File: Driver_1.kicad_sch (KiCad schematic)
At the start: 34 parts

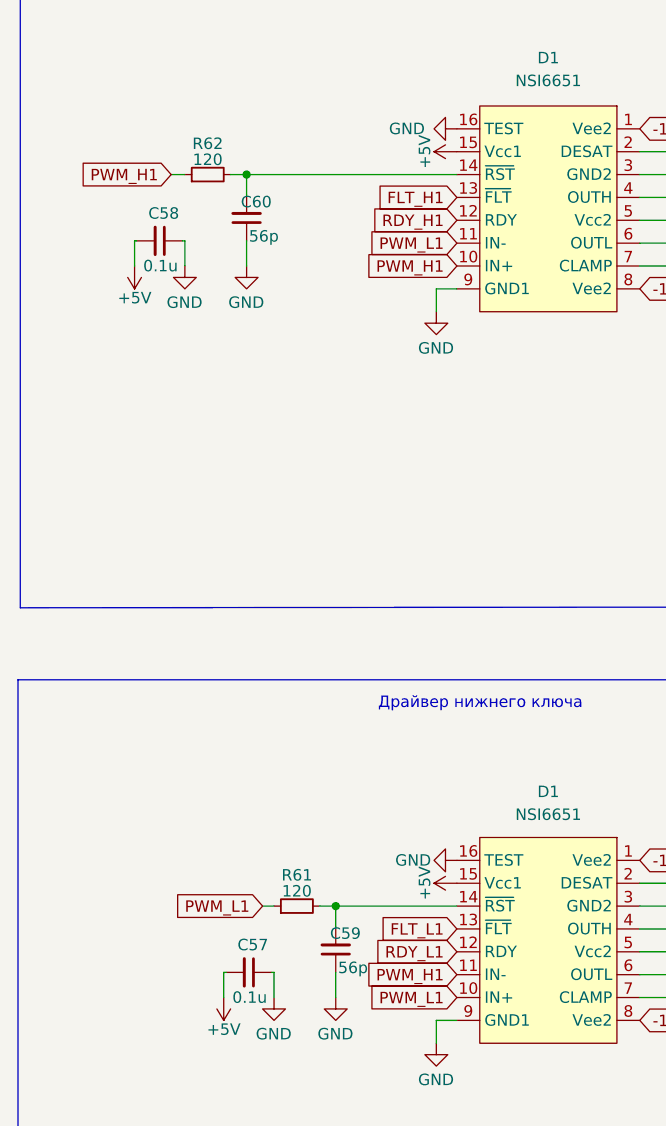
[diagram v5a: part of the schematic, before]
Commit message: Развел стойку фазы А
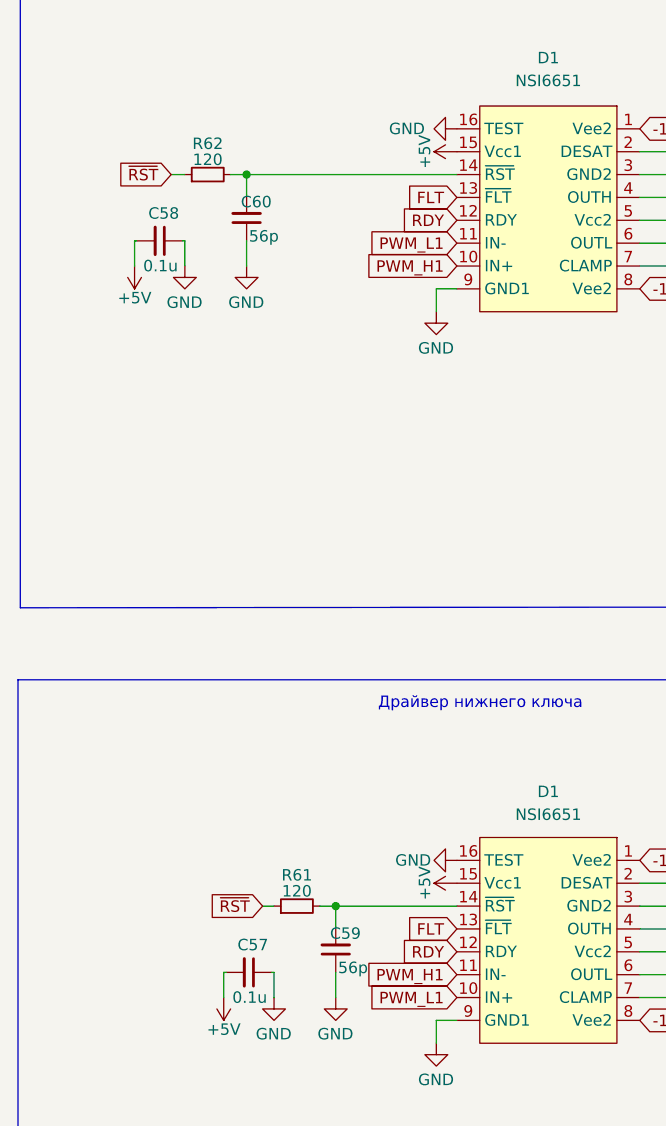
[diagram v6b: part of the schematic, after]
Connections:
- net FLT_L1 is gone; now on net FLT: D1.13 (~{FLT})
- net RDY_L1 is gone; now on net RDY: D1.12 (RDY)
- net PWM_H1: no longer R62.1
- net PWM_L1: no longer R61.1
- net FLT_H1 renamed FLT
- net RDY_H1 renamed RDY
- new net ~{RST}: R61.1, R62.1
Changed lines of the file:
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@@
 		)
 	)
-	(global_label "PWM_H1"
+	(global_label "~{RST}"
 		(shape input)
 		(at 48.26 52.07 180)
@@
 		)
 		(property "Intersheetrefs" "${INTERSHEET_REFS}"
-			(at 38.1664 51.9906 0)
+			(at 42.445 52.07 0)
 			(effects
 				(font
@@
 		)
 	)
-	(global_label "RDY_H1"
+	(global_label "RDY"
 		(shape input)
 		(at 80.01 57.15 180)
@@
 		)
 		(property "Intersheetrefs" "${INTERSHEET_REFS}"
-			(at 70.4607 57.0706 0)
+			(at 74.0684 57.15 0)
 			(effects
 				(font
@@
 		)
 	)
-	(global_label "PWM_L1"
-		(shape input)
-		(at 58.42 133.35 180)
-		(fields_autoplaced yes)
-		(effects
-			(font
-				(size 1.27 1.27)
-			)
-			(justify right)
-		)
-		(property "Intersheetrefs" "${INTERSHEET_REFS}"
-			(at 48.6288 133.2706 0)
-			(effects
-				(font
-					(size 1.27 1.27)
-				)
-				(justify right)
-				(hide yes)
-			)
-		)
-	)
 	(global_label "G1"
 		(shape output)
@@
 		)
 	)
-	(global_label "FLT_H1"
+	(global_label "FLT"
 		(shape input)
 		(at 80.01 54.61 180)
@@
 		)
 		(property "Intersheetrefs" "${INTERSHEET_REFS}"
-			(at 71.005 54.5306 0)
+			(at 74.4506 54.61 0)
 			(effects
 				(font
@@
 		)
 	)
-	(global_label "FLT_L1"
+	(global_label "FLT"
 		(shape input)
 		(at 80.01 135.89 180)
@@
 		)
 		(property "Intersheetrefs" "${INTERSHEET_REFS}"
-			(at 71.3074 135.8106 0)
+			(at 74.4506 135.89 0)
+			(effects
+				(font
+					(size 1.27 1.27)
+				)
+				(justify right)
+				(hide yes)
+			)
+		)
+	)
+	(global_label "~{RST}"
+		(shape input)
+		(at 58.42 133.35 180)
+		(fields_autoplaced yes)
+		(effects
+			(font
+				(size 1.27 1.27)
+			)
+			(justify right)
+		)
+		(property "Intersheetrefs" "${INTERSHEET_REFS}"
+			(at 52.605 133.35 0)
 			(effects
 				(font
@@
 		)
 	)
-	(global_label "RDY_L1"
+	(global_label "RDY"
 		(shape input)
 		(at 80.01 138.43 180)
@@
 		)
 		(property "Intersheetrefs" "${INTERSHEET_REFS}"
-			(at 70.7631 138.3506 0)
+			(at 74.0684 138.43 0)
 			(effects
 				(font
@@
 		(on_board yes)
 		(dnp no)
-		(property "Reference" "#PWR168"
+		(property "Reference" "#PWR0168"
 			(at 83.82 49.53 0)
 			(effects
@@
 			(project "Adapter"
 				(path "/e63e39d7-6ac0-4ffd-8aa3-1841a4541b55/24ca47b2-866f-4c90-ba1b-98c358d573e6"
-					(reference "#PWR168")
+					(reference "#PWR0168")
 					(unit 1)
 				)
@@
 		(on_board yes)
 		(dnp no)
-		(property "Reference" "#PWR162"
+		(property "Reference" "#PWR0162"
 			(at 83.82 130.81 0)
 			(effects
@@
 			(project "Adapter"
 				(path "/e63e39d7-6ac0-4ffd-8aa3-1841a4541b55/24ca47b2-866f-4c90-ba1b-98c358d573e6"
-					(reference "#PWR162")
+					(reference "#PWR0162")
 					(unit 1)
 				)
@@
 		(on_board yes)
 		(dnp no)
-		(property "Reference" "#PWR167"
+		(property "Reference" "#PWR0167"
 			(at 44.196 58.42 0)
 			(effects
@@
 			(project "Adapter"
 				(path "/e63e39d7-6ac0-4ffd-8aa3-1841a4541b55/24ca47b2-866f-4c90-ba1b-98c358d573e6"
-					(reference "#PWR167")
+					(reference "#PWR0167")
 					(unit 1)
 				)
@@
 		(on_board yes)
 		(dnp no)
-		(property "Reference" "#PWR161"
+		(property "Reference" "#PWR0161"
 			(at 54.102 139.7 0)
 			(effects
@@
 			(project "Adapter"
 				(path "/e63e39d7-6ac0-4ffd-8aa3-1841a4541b55/24ca47b2-866f-4c90-ba1b-98c358d573e6"
-					(reference "#PWR161")
-					(unit 1)
-				)
+					(reference "#PWR0161")
+					(unit 1)
+				)

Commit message: Развел вторую стойку
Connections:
- net FLT renamed FLT_A
- net RDY renamed RDY_A
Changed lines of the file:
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@@
 		)
 	)
-	(global_label "RDY"
+	(global_label "RDY_A"
 		(shape input)
 		(at 80.01 57.15 180)
@@
 		)
 		(property "Intersheetrefs" "${INTERSHEET_REFS}"
-			(at 74.0684 57.15 0)
+			(at 71.34 57.15 0)
 			(effects
 				(font
@@
 		)
 	)
-	(global_label "FLT"
+	(global_label "FLT_A"
 		(shape input)
 		(at 80.01 54.61 180)
@@
 		)
 		(property "Intersheetrefs" "${INTERSHEET_REFS}"
-			(at 74.4506 54.61 0)
-			(effects
-				(font
-					(size 1.27 1.27)
-				)
-				(justify right)
-				(hide yes)
-			)
-		)
-	)
-	(global_label "FLT"
+			(at 71.8843 54.61 0)
+			(effects
+				(font
+					(size 1.27 1.27)
+				)
+				(justify right)
+				(hide yes)
+			)
+		)
+	)
+	(global_label "FLT_A"
 		(shape input)
 		(at 80.01 135.89 180)
@@
 		)
 		(property "Intersheetrefs" "${INTERSHEET_REFS}"
-			(at 74.4506 135.89 0)
+			(at 71.8843 135.89 0)
 			(effects
 				(font
@@
 		)
 	)
-	(global_label "RDY"
+	(global_label "RDY_A"
 		(shape input)
 		(at 80.01 138.43 180)
@@
 		)
 		(property "Intersheetrefs" "${INTERSHEET_REFS}"
-			(at 74.0684 138.43 0)
-			(effects
-				(font
+			(at 71.34 138.43 0)
+			(effects
+				(font
